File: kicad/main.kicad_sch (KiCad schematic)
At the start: 11 parts, among them J1 Barrel_Jack, U1 74HC573, U2 27C512, U3 AS6C4008-55PCN, U4 KM1810VM88, U5 74HC573, U6 ATF16V8, U7 74LS73, U8 L7805, X1 15 MHz

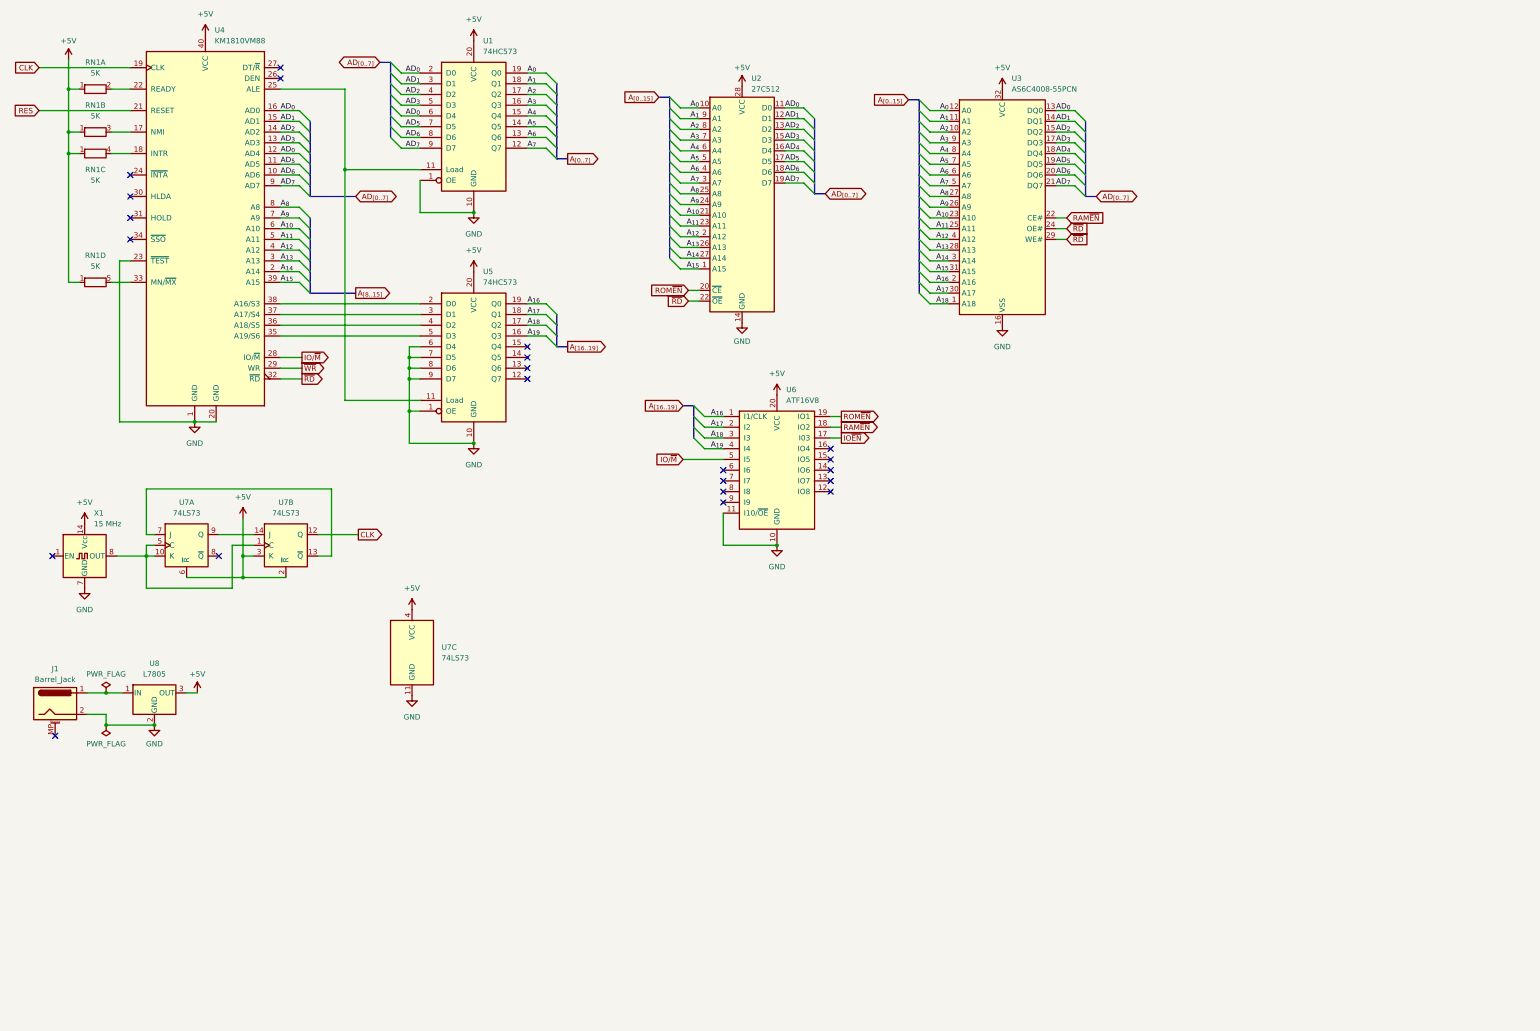
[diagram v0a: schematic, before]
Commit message: First prototype without I/O
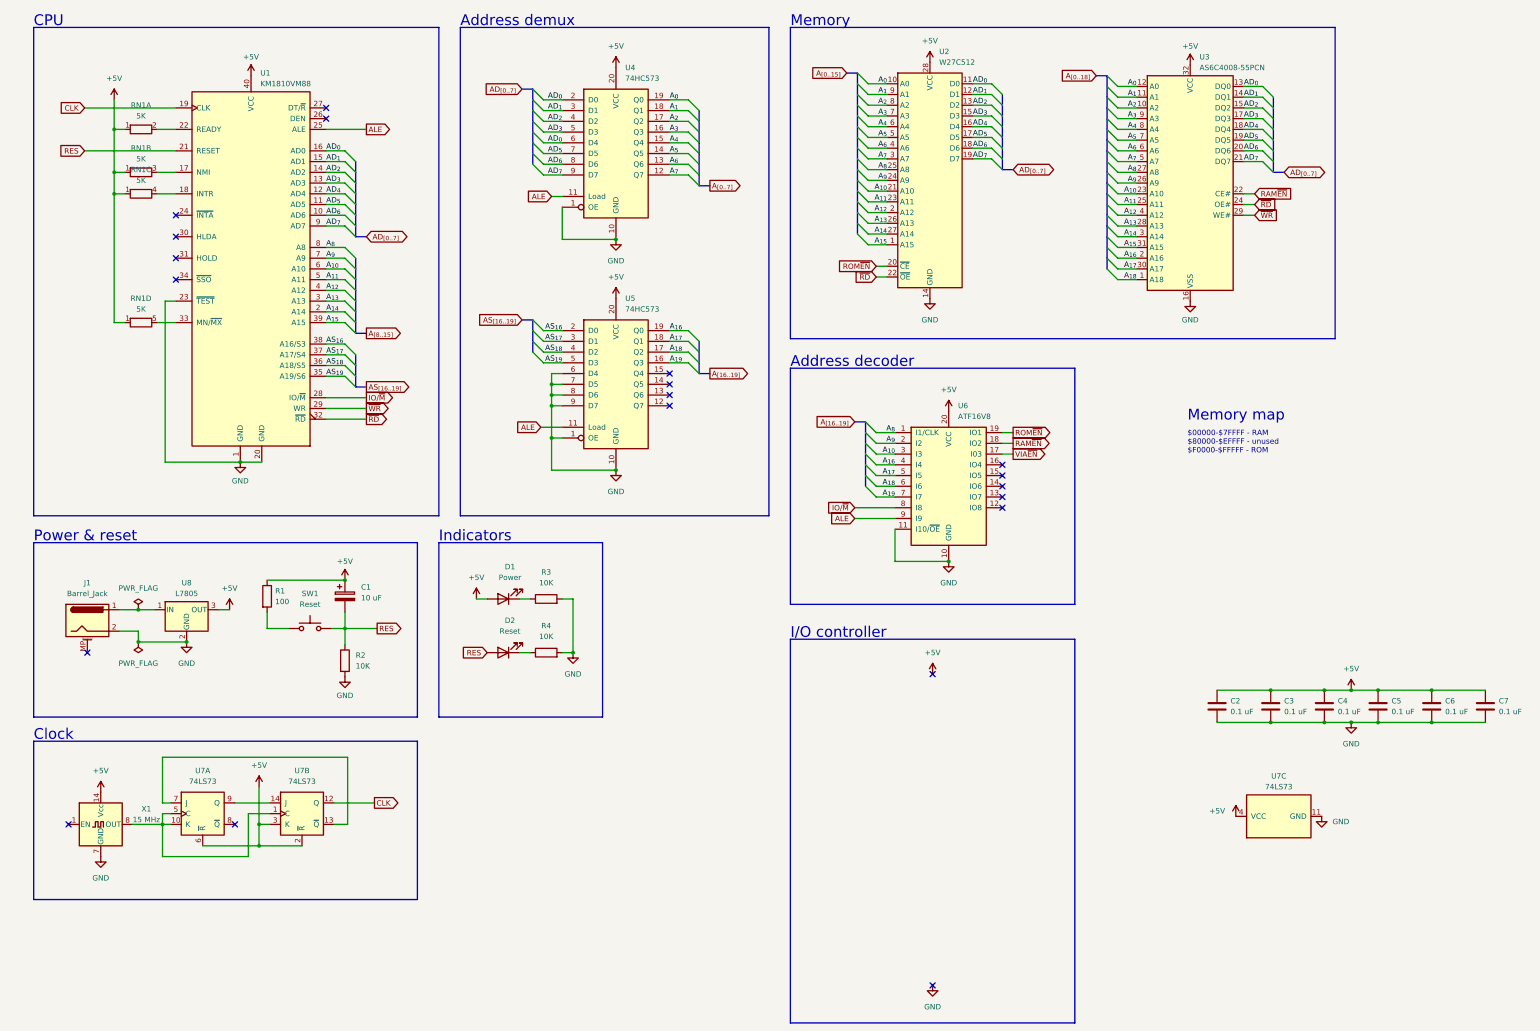
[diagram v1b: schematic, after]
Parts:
- added C1: 10 uF, symbol Device:C_Polarized
- added C2, C3, C4, C5, C6, C7: 0.1 uF, symbol Device:C
- added D1: Power, symbol Device:LED
- added D2: Reset, symbol Device:LED
- added R1: 100, symbol Device:R
- added R2, R3, R4: 10K, symbol Device:R
- added SW1: Reset, symbol Switch:SW_Push
- U2: value 27C512 -> W27C512
- renumbered U4 to U1, U1 to U4
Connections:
- net +5V: now also C1.1, C2.1, C3.1, C4.1, C5.1, C6.1, C7.1, D1.2 (A), R1.1
- net AD_{0}: no longer U1.12 (AD4)
- net AD_{4}: now also U1.12 (AD4)
- net A_{10}: now also U6.3 (I3)
- net A_{16}: now also U6.4 (I4); no longer U6.1 (I1/CLK)
- net A_{17}: now also U6.5 (I5); no longer U6.2 (I2)
- net A_{18}: now also U6.6 (I6); no longer U6.3 (I3)
- net A_{19}: now also U6.7 (I7); no longer U6.4 (I4)
- net A_{8}: now also U6.1 (I1/CLK)
- net A_{9}: now also U6.2 (I2)
- net GND: now also C2.2, C3.2, C4.2, C5.2, C6.2, C7.2, R2.2, R3.2, R4.2
- net IO/~{M}: now also U6.8 (I8); no longer U6.5 (I5)
- net RES: now also C1.2, D2.2 (A), R2.1, SW1.2
- net ~{RD}: no longer U3.29 (WE#)
- net ~{WR}: now also U3.29 (WE#)
- net ALE: now reaches U6.9 (I9)
- net ALE: now also U1.25 (ALE), U4.11 (Load), U5.11 (Load)
- net AS_{16}: now reaches U1.38 (A16/S3), U5.2 (D0)
- net AS_{17}: now reaches U1.37 (A17/S4), U5.3 (D1)
- net AS_{18}: now reaches U1.36 (A18/S5), U5.4 (D2)
- net AS_{19}: now reaches U1.35 (A19/S6), U5.5 (D3)
- net IO~{EN} renamed VIA~{EN}
- new net: D1.1 (K), R3.1
- new net: D2.1 (K), R4.1
- new net: R1.2, SW1.1
- no-connect marks 22 -> 20
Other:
- note added: "$00000-$7FFFF - RAM $80000-$EFFFF - unused $F0000-$FFFFF - ROM"
- note added: "Address decoder"
- note added: "Address demux"
- note added: "CPU"
- note added: "Clock"
- note added: "I/O controller"
- note added: "Indicators"
- note added: "Memory"
- note added: "Memory map"
- note added: "Power & reset"
- moved on the sheet: J1, RN1A, RN1B, RN1C, RN1D, U1, U2, U3, U4, U6, U7A, U7B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

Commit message: Add interrupt controller & display
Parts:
- added C8, C9: 0.1 uF, Capacitor_THT:C_Disc_D3.0mm_W1.6mm_P2.50mm, symbol Device:C
- added LCD1: ~, footprints:2004A-OLED, symbol lcd:2004A-OLED
- added RN2: R_Network08, Resistor_THT:R_Array_SIP9, symbol Device:R_Network08
- added SW2: A, Button_Switch_THT:SW_PUSH_6mm_H5mm, symbol Switch:SW_Push
- added SW3: B, Button_Switch_THT:SW_PUSH_6mm_H5mm, symbol Switch:SW_Push
- added SW4: C, Button_Switch_THT:SW_PUSH_6mm_H5mm, symbol Switch:SW_Push
- added SW5: D, Button_Switch_THT:SW_PUSH_6mm_H5mm, symbol Switch:SW_Push
- added SW6: E, Button_Switch_THT:SW_PUSH_6mm_H5mm, symbol Switch:SW_Push
- added SW7: F, Button_Switch_THT:SW_PUSH_6mm_H5mm, symbol Switch:SW_Push
- added SW8: G, Button_Switch_THT:SW_PUSH_6mm_H5mm, symbol Switch:SW_Push
- added SW9: H, Button_Switch_THT:SW_PUSH_6mm_H5mm, symbol Switch:SW_Push
- added U7: 74HC148, Package_DIP:DIP-16_W7.62mm_Socket, symbol 74xx:74LS148
- added U8: 74HC00, Package_DIP:DIP-14_W7.62mm_Socket, symbol 74xx:74HC00
- added U9: 74HC244, Package_DIP:DIP-20_W7.62mm_Socket, symbol 74xx:74HC244
- C1: footprint (none) -> Capacitor_THT:CP_Radial_D5.0mm_P2.50mm
- C2, C3, C4, C5, C6, C7: footprint (none) -> Capacitor_THT:C_Disc_D3.0mm_W1.6mm_P2.50mm
- D1, D2: footprint (none) -> LED_THT:LED_D3.0mm
- R1: footprint (none) -> Resistor_THT:R_Axial_DIN0204_L3.6mm_D1.6mm_P7.62mm_Horizontal
- R2: renamed from R3; footprint (none) -> Resistor_THT:R_Axial_DIN0204_L3.6mm_D1.6mm_P7.62mm_Horizontal
- R3: renamed from R4; footprint (none) -> Resistor_THT:R_Axial_DIN0204_L3.6mm_D1.6mm_P7.62mm_Horizontal
- R4: renamed from R2; footprint (none) -> Resistor_THT:R_Axial_DIN0204_L3.6mm_D1.6mm_P7.62mm_Horizontal
- SW1: footprint (none) -> Button_Switch_THT:SW_PUSH_6mm_H5mm
- renumbered U8 to U10, U7 to U11
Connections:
- net +5V: now also C8.1, C9.1, LCD1.2 (Vdd), RN2.1 (common), U7.16 (VCC), U8.14 (VCC), U9.20 (VCC)
- net AD_{0}: now also LCD1.4 (RS), LCD1.7 (D_{0}), U9.18 (1Y0); no longer U4.6 (D4)
- net AD_{1}: now also LCD1.8 (D_{1}), U9.16 (1Y1)
- net AD_{2}: now also LCD1.9 (D_{2}), U9.14 (1Y2)
- net AD_{3}: now also LCD1.10 (D_{3}), U9.12 (1Y3)
- net AD_{4}: now also U4.6 (D4), LCD1.11 (D_{4}), U9.3 (2Y0)
- net AD_{5}: now also LCD1.12 (D_{5}), U9.5 (2Y1)
- net AD_{6}: now also LCD1.13 (D_{6}), U9.7 (2Y2)
- net AD_{7}: now also LCD1.14 (D_{7}), U9.9 (2Y3)
- net GND: now also C8.2, C9.2, LCD1.1 (GND), SW2.1, SW3.1, SW4.1, SW5.1, SW6.1, SW7.1, SW8.1, SW9.1, U7.5 (EI), U7.8 (GND), U8.7 (GND), U9.10 (GND), U9.11 (2A3), U9.13 (2A2), U9.15 (2A1), U9.17 (2A0), U9.8 (1A3)
- net ~{WR}: now also LCD1.5 (R~{W})
- net at RN1.4 (R3.2): now also U1.33 (MN/~{MX}); no longer U1.18 (INTR)
- net ~{INTA}: now reaches U1.24 (~{INTA})
- net ~{INTA}: now also U9.1 (1OE), U9.19 (2OE)
- net at RN1.5 (R4.2): no longer U1.33 (MN/~{MX})
- net VIA~{EN} renamed LCDEN
- net LCDEN: now also LCD1.6 (E)
- new net: U7.9 (S0), U9.2 (1A0)
- new net: U7.7 (S1), U9.4 (1A1)
- new net: U7.6 (S2), U9.6 (1A2)
- new net: U7.14 (GS), U8.1, U8.2
- new net INTR: U1.18 (INTR), U8.3
- new net ~{INT0}: RN2.2 (R1), SW2.2, U7.4 (I7)
- new net ~{INT1}: RN2.3 (R2), SW3.2, U7.3 (I6)
- new net ~{INT2}: RN2.4 (R3), SW4.2, U7.2 (I5)
- new net ~{INT3}: RN2.5 (R4), SW5.2, U7.1 (I4)
- new net ~{INT4}: RN2.6 (R5), SW6.2, U7.13 (I3)
- new net ~{INT5}: RN2.7 (R6), SW7.2, U7.12 (I2)
- new net ~{INT6}: RN2.8 (R7), SW8.2, U7.11 (I1)
- new net ~{INT7}: RN2.9 (R8), SW9.2, U7.10 (IO)
- no-connect marks 20 -> 30
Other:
- note added: "$00000-$7FFFF - RAM $80000-$EFFFF - unused $F0000-$FFFFF - ROM Ports: $0000 - $00FF - LCD"
- note added: "Buttons"
- note added: "Interrupt controller"
- note added: "OLED display"
- note removed: "$00000-$7FFFF - RAM $80000-$EFFFF - unused $F0000-$FFFFF - ROM"
- moved on the sheet: C2, C3, C4, C5, C6, C7, RN1A, RN1B, RN1D, U1, U11C

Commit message: Add parallel port
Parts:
- removed RN2: R_Network08, Resistor_THT:R_Array_SIP9, symbol Device:R_Network08
- removed SW6: E, Button_Switch_THT:SW_PUSH_6mm_H5mm, symbol Switch:SW_Push
- removed SW7: F, Button_Switch_THT:SW_PUSH_6mm_H5mm, symbol Switch:SW_Push
- removed SW8: G, Button_Switch_THT:SW_PUSH_6mm_H5mm, symbol Switch:SW_Push
- removed SW9: H, Button_Switch_THT:SW_PUSH_6mm_H5mm, symbol Switch:SW_Push
- removed U11: 74LS73, Package_DIP:DIP-14_W7.62mm_Socket, symbol 74xx:74LS73
- removed U8: 74HC00, Package_DIP:DIP-14_W7.62mm_Socket, symbol 74xx:74HC00
- removed X1: 15 MHz, Oscillator:Oscillator_DIP-14, symbol Oscillator:CXO_DIP14
- added C10: 0.1 uF, Capacitor_THT:C_Disc_D3.0mm_W1.6mm_P2.50mm, symbol Device:C
- added RN2: R_Network04, Resistor_THT:R_Array_SIP5, symbol Device:R_Network04
- added U11: 15 MHz, footprints:Oscillator_DIP-8-14, symbol my:CXO_DIP-8-14
- added U12: 8255, Package_DIP:DIP-40_W15.24mm_Socket, symbol Interface:8255
- added U8: 74HC00, Package_DIP:DIP-14_W7.62mm_Socket, symbol 74hc00_small:74HC00
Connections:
- net ~{INT4} is gone; now on net +5V: U7.13 (I3)
- net ~{INT5} is gone; now on net +5V: U7.12 (I2)
- net ~{INT6} is gone; now on net +5V: U7.11 (I1)
- net ~{INT7} is gone; now on net +5V: U7.10 (IO)
- net +5V: now also C10.1, RN2.1 (common), U11.12, U11.13, U11.14 (Vcc), U12.26 (VCC), U8.14 (VCC)
- net AD_{0}: now also U12.34 (D0); no longer LCD1.4 (RS), LCD1.7 (D_{0})
- net AD_{1}: now also U12.33 (D1); no longer LCD1.8 (D_{1})
- net AD_{2}: now also U12.32 (D2); no longer LCD1.9 (D_{2})
- net AD_{3}: now also U12.31 (D3); no longer LCD1.10 (D_{3})
- net AD_{4}: now also U12.30 (D4); no longer LCD1.11 (D_{4})
- net AD_{5}: now also U12.29 (D5); no longer LCD1.12 (D_{5})
- net AD_{6}: now also U12.28 (D6); no longer LCD1.13 (D_{6})
- net AD_{7}: now also U12.27 (D7); no longer LCD1.14 (D_{7})
- net ALE: no longer U6.9 (I9)
- net A_{0}: now also U12.9 (A0)
- net A_{10}: now also U6.4 (I4); no longer U6.3 (I3)
- net A_{16}: now also U6.5 (I5); no longer U6.4 (I4)
- net A_{17}: now also U6.6 (I6); no longer U6.5 (I5)
- net A_{18}: now also U6.7 (I7); no longer U6.6 (I6)
- net A_{19}: now also U6.8 (I8); no longer U6.7 (I7)
- net A_{1}: now also U12.8 (A1)
- net A_{8}: now also U6.2 (I2); no longer U6.1 (I1/CLK)
- net A_{9}: now also U6.3 (I3); no longer U6.2 (I2)
- net CLK: now also U8.6
- net GND: now also C10.2, U11.5, U11.6, U11.7 (GND), U12.7 (GND), U8.7 (GND)
- net INTR: now also U8.3
- net IO/~{M}: now also U6.9 (I9); no longer U6.8 (I8)
- net ~{INT0}: now also RN2.2 (R1)
- net ~{INT1}: now also RN2.3 (R2)
- net ~{INT2}: now also RN2.4 (R3)
- net ~{INT3}: now also RN2.5 (R4)
- net ~{RD}: now also U12.5 (~{RD})
- net ~{WR}: now also U12.36 (~{WR}); no longer LCD1.5 (R~{W})
- net at U6.13 (IO7): now also U8.4, U8.5
- net at U7.14 (GS): now also U8.1, U8.2
- net LCDEN: no longer names the net of LCD1.6 (E)
- net LCDEN: now also U12.20 (PB2); no longer U6.17 (I03)
- new net: U11.10, U11.8 (OUT), U11.9, U6.1 (I1/CLK)
- new net: LCD1.10 (D_{3}), U12.1 (PA3)
- new net: LCD1.4 (RS), U12.18 (PB0)
- new net: LCD1.5 (R~{W}), U12.19 (PB1)
- new net: LCD1.9 (D_{2}), U12.2 (PA2)
- new net: LCD1.8 (D_{1}), U12.3 (PA1)
- new net: LCD1.14 (D_{7}), U12.37 (PA7)
- new net: LCD1.13 (D_{6}), U12.38 (PA6)
- new net: LCD1.12 (D_{5}), U12.39 (PA5)
- new net: LCD1.7 (D_{0}), U12.4 (PA0)
- new net: LCD1.11 (D_{4}), U12.40 (PA4)
- new net IO~{EN}: U12.35 (RESET), U12.6 (~{CS}), U6.17 (I03)
- no-connect marks 30 -> 38
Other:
- note added: "Address decoder & clock generator"
- note removed: "Address decoder"
- note removed: "Clock"
- note removed: "OLED display"
- moved on the sheet: C1, C2, C3, C4, C5, C6, C7, C8, C9, D1, D2, J1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

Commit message: Add Freerouting PCB
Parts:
- removed C1: 10 uF, Capacitor_THT:CP_Radial_D5.0mm_P2.50mm, symbol Device:C_Polarized
- removed R1: 100, Resistor_THT:R_Axial_DIN0204_L3.6mm_D1.6mm_P7.62mm_Horizontal, symbol Device:R
- removed R4: 10K, Resistor_THT:R_Axial_DIN0204_L3.6mm_D1.6mm_P7.62mm_Horizontal, symbol Device:R
- removed RN2: R_Network04, Resistor_THT:R_Array_SIP5, symbol Device:R_Network04
- removed SW2: A, Button_Switch_THT:SW_PUSH_6mm_H5mm, symbol Switch:SW_Push
- removed SW3: B, Button_Switch_THT:SW_PUSH_6mm_H5mm, symbol Switch:SW_Push
- removed SW4: C, Button_Switch_THT:SW_PUSH_6mm_H5mm, symbol Switch:SW_Push
- removed SW5: D, Button_Switch_THT:SW_PUSH_6mm_H5mm, symbol Switch:SW_Push
- removed U7: 74HC148, Package_DIP:DIP-16_W7.62mm_Socket, symbol 74xx:74LS148
- removed unit 1 of U8
- removed U9: 74HC244, Package_DIP:DIP-20_W7.62mm_Socket, symbol 74xx:74HC244
- added BAR1: HDSP-4830_2, Display:HDSP-4830, symbol LED:HDSP-4830_2
- added C11: 0.1 uF, Capacitor_THT:C_Disc_D3.0mm_W1.6mm_P2.50mm, symbol Device:C
- added H1, H2: MountingHole, footprints:Hole_2.5x4, symbol Mechanical:MountingHole
- added RN2: 330R, Resistor_THT:R_Array_SIP9, symbol Device:R_Network08
- added RN3: 5K, Resistor_THT:R_Array_SIP9, symbol Device:R_Network08
- added SW2: SW_DIP_x08, Button_Switch_THT:SW_DIP_SPSTx08_Slide_9.78x22.5mm_W7.62mm_P2.54mm, symbol Switch:SW_DIP_x08
- added U6: 74HC273, Package_DIP:DIP-20_W7.62mm_Socket, symbol 74xx:74HC273
- added U7: DS1813-5+, Package_TO_SOT_THT:TO-92L_Inline_Wide, symbol ds1813:DS1813-5+
- added U8: 74HC244, Package_DIP:DIP-20_W7.62mm_Socket, symbol 74xx:74HC244
- added unit 3 of U8
- C10, C2, C4, C5, C7, C8, C9: footprint Capacitor_THT:C_Disc_D3.0mm_W1.6mm_P2.50mm -> footprints:C_Disc_Long
- C6: footprint Capacitor_THT:C_Disc_D3.0mm_W1.6mm_P2.50mm -> footprints:C_Disc_VeryLong
- U2: footprint Package_DIP:DIP-28_W15.24mm -> footprints:ZIF28
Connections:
- net INTR is gone; now on an unnamed net: U1.18 (INTR)
- net +5V: now also C11.1, SW2.1, SW2.2, SW2.3, SW2.4, SW2.5, SW2.6, SW2.7, SW2.8, U6.20 (VCC), U7.2 (VCC), U8.20 (VCC)
- net AD_{0}: now also U4.9 (D7), U6.3 (D0), U8.18 (1Y0); no longer U4.2 (D0)
- net AD_{1}: now also U4.8 (D6), U6.4 (D1), U8.16 (1Y1); no longer U4.3 (D1)
- net AD_{2}: now also U4.7 (D5), U6.7 (D2), U8.14 (1Y2); no longer U4.4 (D2)
- net AD_{3}: now also U4.6 (D4), U6.8 (D3), U8.12 (1Y3); no longer U4.5 (D3)
- net AD_{4}: now also U4.5 (D3), U6.13 (D4), U8.3 (2Y0); no longer U4.6 (D4)
- net AD_{5}: now also U4.4 (D2), U6.14 (D5), U8.5 (2Y1); no longer U4.7 (D5)
- net AD_{6}: now also U4.3 (D1), U6.17 (D6), U8.7 (2Y2); no longer U4.8 (D6)
- net AD_{7}: now also U4.2 (D0), U6.18 (D7), U8.9 (2Y3); no longer U4.9 (D7)
- net A_{0}: now also U4.12 (Q7); no longer U4.19 (Q0)
- net A_{10}: no longer U6.4 (I4)
- net A_{16}: now also U6.3 (I3); no longer U6.5 (I5)
- net A_{17}: now also U6.4 (I4); no longer U6.6 (I6)
- net A_{18}: now also U6.5 (I5); no longer U6.7 (I7)
- net A_{19}: now also U6.6 (I6); no longer U6.8 (I8)
- net A_{1}: now also U4.13 (Q6); no longer U4.18 (Q1)
- net A_{2}: now also U4.14 (Q5); no longer U4.17 (Q2)
- net A_{3}: now also U4.15 (Q4); no longer U4.16 (Q3)
- net A_{4}: now also U4.16 (Q3); no longer U4.15 (Q4)
- net A_{5}: now also U4.17 (Q2); no longer U4.14 (Q5)
- net A_{6}: now also U4.18 (Q1); no longer U4.13 (Q6)
- net A_{7}: now also U4.19 (Q0); no longer U4.12 (Q7)
- net A_{9}: no longer U6.3 (I3)
- net CLK: now also U8.3; no longer U8.6
- net GND: now also SW1.2, C11.2, RN2.1 (common), RN3.1 (common), U6.10 (GND), U7.3 (GND), U8.10 (GND)
- net IO~{EN}: now also U6.15 (IO5); no longer U12.35 (RESET), U6.17 (I03)
- net RES: now also U12.35 (RESET), U8.4, U8.5, U8.8; no longer SW1.2
- net ~{RD}: now also U6.7 (I7)
- net ~{WR}: now also U6.8 (I8)
- net IN~{EN}: now reaches U6.16 (IO4)
- net IN~{EN}: now also U8.1 (1OE), U8.19 (2OE)
- net at RN1.4 (R3.2): no longer U1.33 (MN/~{MX})
- net at SW1.1: now also U7.1 (~{RST}), U8.10, U8.9
- net at RN1.5 (R4.2): now also U1.33 (MN/~{MX})
- net ~{INTA}: no longer names the net of U1.24 (~{INTA})
- new net: U6.13 (IO7), U8.1, U8.2
- new net: RN3.2 (R1), SW2.16, U8.2 (1A0)
- new net: RN3.3 (R2), SW2.15, U8.4 (1A1)
- new net: RN3.4 (R3), SW2.14, U8.6 (1A2)
- new net: RN3.5 (R4), SW2.13, U8.8 (1A3)
- new net: RN3.6 (R5), SW2.12, U8.17 (2A0)
- new net: RN3.7 (R6), SW2.11, U8.15 (2A1)
- new net: RN3.8 (R7), SW2.10, U8.13 (2A2)
- new net: RN3.9 (R8), SW2.9, U8.11 (2A3)
- new net: U6.1 (~{Mr}), U8.6
- new net: BAR1.5 (A), U6.12 (Q4)
- new net: BAR1.6 (A), U6.15 (Q5)
- new net: BAR1.7 (A), U6.16 (Q6)
- new net: BAR1.8 (A), U6.19 (Q7)
- new net: BAR1.1 (A), U6.2 (Q0)
- new net: BAR1.2 (A), U6.5 (Q1)
- new net: BAR1.3 (A), U6.6 (Q2)
- new net: BAR1.4 (A), U6.9 (Q3)
- new net: BAR1.20 (K), RN2.2 (R1)
- new net: BAR1.19 (K), RN2.3 (R2)
- new net: BAR1.18 (K), RN2.4 (R3)
- new net: BAR1.17 (K), RN2.5 (R4)
- new net: BAR1.16 (K), RN2.6 (R5)
- new net: BAR1.15 (K), RN2.7 (R6)
- new net: BAR1.14 (K), RN2.8 (R7)
- new net: BAR1.13 (K), RN2.9 (R8)
- new net OUT~{EN}: U6.11 (Cp), U6.17 (I03)
- no-connect marks 38 -> 36
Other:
- note added: "I/O register"
- note removed: "Buttons"
- note removed: "Interrupt controller"
- moved on the sheet: C10, C2, C3, C4, C5, C6, C7, C8, C9, J1, RN1C, RN1D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
